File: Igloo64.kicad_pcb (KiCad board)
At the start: 2 copper layers, 96.5 x 90.2 mm, 31 parts, among them J1 Conn_02x32_Counter_Clockwise, J10 Conn_01x32, J11 Conn_01x02, J12 Conn_01x02, J13 Conn_01x02, J14 Conn_01x02, J15 Conn_01x02, J16 Conn_01x02, J17 Conn_01x02, J18 Conn_01x02, J19 Conn_01x02, J2 Conn_02x16_Odd_Even, J3 Conn_02x16_Odd_Even, J4 Conn_02x16_Odd_Even, J5 Conn_02x16_Odd_Even, J6 Conn_02x32_Odd_Even, J7 Conn_02x32_Odd_Even, J8 Conn_02x32_Odd_Even, J9 Conn_01x32

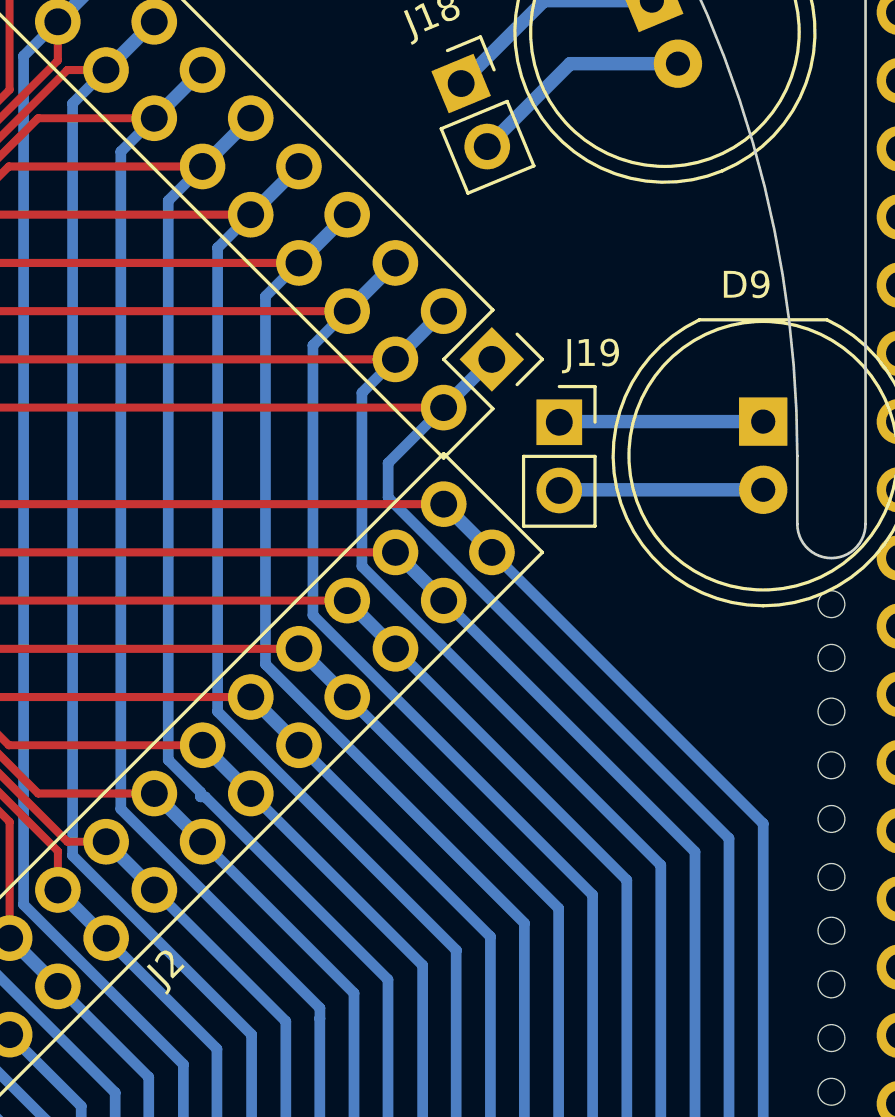
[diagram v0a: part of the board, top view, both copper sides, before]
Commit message: Fix DRC error.
One track too close to pin. Evened out some of the rear tracks for neatness.
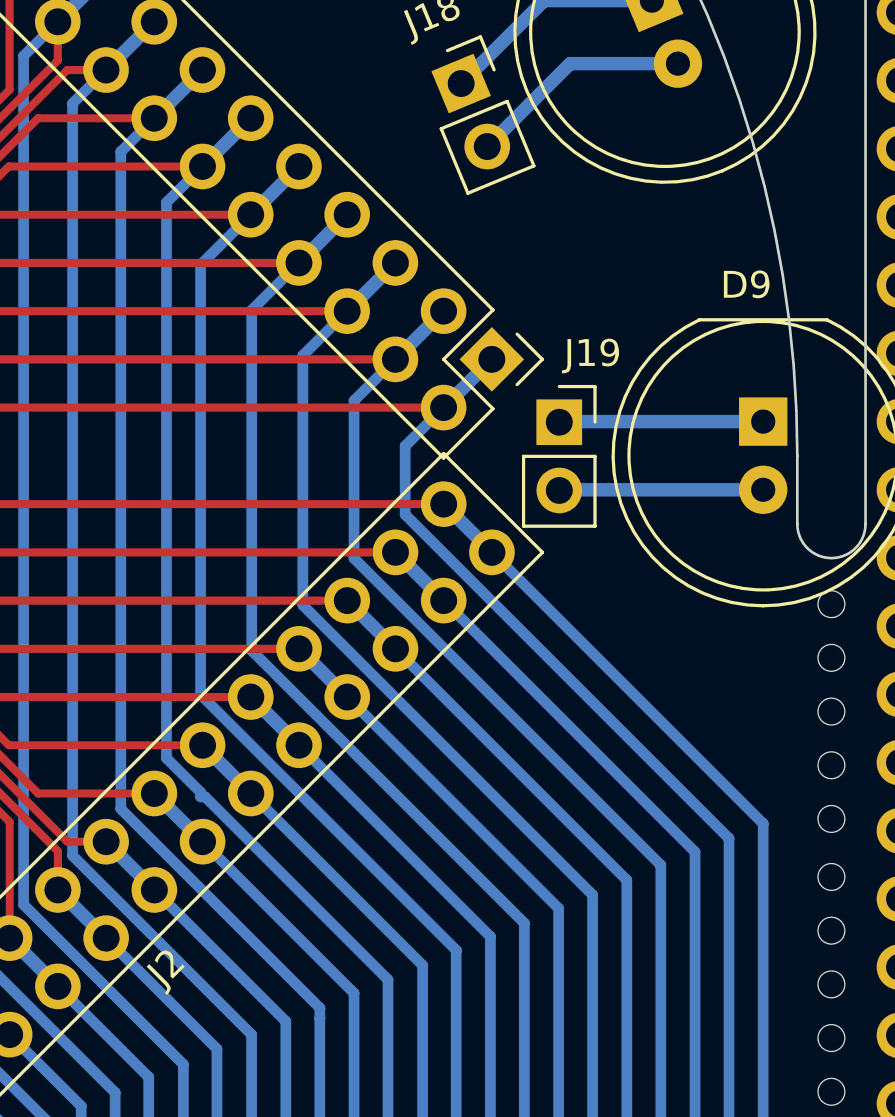
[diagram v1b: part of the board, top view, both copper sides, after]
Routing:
- net /pin37: track 82.1 -> 82.6 mm
- net /pin33: track 80.2 -> 79.7 mm
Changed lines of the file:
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@@
 	)
 	(segment
-		(start 158.75 90.454258)
-		(end 158.75 89.170769)
+		(start 159.385 91.089258)
+		(end 159.385 88.535769)
 		(width 0.4)
 		(layer "B.Cu")
@@
 	)
 	(segment
-		(start 171.445 125.735)
-		(end 171.445 103.149258)
+		(start 171.445 103.149258)
+		(end 159.385 91.089258)
 		(width 0.4)
 		(layer "B.Cu")
@@
 	)
 	(segment
-		(start 171.445 103.149258)
-		(end 158.75 90.454258)
+		(start 171.445 125.735)
+		(end 171.445 103.149258)
 		(width 0.4)
 		(layer "B.Cu")
@@
 	)
 	(segment
-		(start 162.612871 85.307898)
+		(start 159.385 88.535769)
 		(end 160.81682 87.103949)
-		(width 0.5)
+		(width 0.4)
 		(layer "B.Cu")
 		(net 4)
 	)
 	(segment
-		(start 158.75 89.170769)
+		(start 162.612871 85.307898)
 		(end 160.81682 87.103949)
-		(width 0.4)
+		(width 0.5)
 		(layer "B.Cu")
 		(net 4)
@@
 	)
 	(segment
-		(start 155.428666 81.715796)
-		(end 154.18269 82.961772)
-		(width 0.4)
-		(layer "B.Cu")
-		(net 22)
-	)
-	(segment
 		(start 157.224717 79.919744)
 		(end 155.428666 81.715795)
@@
 	)
 	(segment
-		(start 154.18269 96.663255)
+		(start 153.67 96.150565)
 		(end 163.825 106.305565)
 		(width 0.4)
@@
 	)
 	(segment
-		(start 154.18269 82.961772)
-		(end 154.18269 96.663255)
+		(start 153.67 83.474462)
+		(end 153.67 96.150565)
 		(width 0.4)
 		(layer "B.Cu")
@@
 	)
 	(segment
+		(start 155.428666 81.715796)
+		(end 153.67 83.474462)
+		(width 0.4)
+		(layer "B.Cu")
+		(net 22)
+	)
+	(segment
 		(start 138.028536 90.959449)
 		(end 141.360777 94.291689)
@@
 	)
 	(segment
-		(start 166.365 105.253463)
-		(end 166.365 125.735)
+		(start 155.575 94.463463)
+		(end 166.365 105.253463)
 		(width 0.4)
 		(layer "B.Cu")
@@
 	(segment
 		(start 157.224717 83.511847)
-		(end 155.949766 84.786798)
+		(end 155.575 85.161564)
 		(width 0.4)
 		(layer "B.Cu")
@@
 	)
 	(segment
-		(start 155.949766 84.786798)
-		(end 155.949766 94.838229)
+		(start 155.575 85.161564)
+		(end 155.575 94.463463)
 		(width 0.4)
 		(layer "B.Cu")
@@
 	)
 	(segment
-		(start 155.949766 94.838229)
-		(end 166.365 105.253463)
+		(start 166.365 105.253463)
+		(end 166.365 125.735)
 		(width 0.4)
 		(layer "B.Cu")
@@
 	)
 	(segment
-		(start 168.905 104.14341)
-		(end 168.905 125.735)
+		(start 157.48 92.71841)
+		(end 168.905 104.14341)
 		(width 0.4)
 		(layer "B.Cu")
@@
 	)
 	(segment
-		(start 157.774793 86.553874)
-		(end 157.774793 93.013203)
+		(start 168.905 104.14341)
+		(end 168.905 125.735)
 		(width 0.4)
 		(layer "B.Cu")
@@
 	)
 	(segment
-		(start 159.020769 85.307898)
-		(end 157.774793 86.553874)
+		(start 157.48 86.848667)
+		(end 157.48 92.71841)
 		(width 0.4)
 		(layer "B.Cu")
@@
 	)
 	(segment
-		(start 157.774793 93.013203)
-		(end 168.905 104.14341)
+		(start 159.020769 85.307898)
+		(end 157.48 86.848667)
 		(width 0.4)
 		(layer "B.Cu")
@@
 	)
 	(segment
-		(start 158.745 108.40977)
-		(end 158.745 125.735)
+		(start 151.765 101.42977)
+		(end 151.765 101.6)
 		(width 0.4)
 		(layer "B.Cu")
@@
 	)
 	(segment
-		(start 150.561613 100.226383)
-		(end 151.765 101.42977)
+		(start 150.495 79.465257)
+		(end 150.495 100.15977)
 		(width 0.4)
 		(layer "B.Cu")
@@
 	)
 	(segment
-		(start 151.836564 78.123693)
-		(end 150.561613 79.398644)
+		(start 158.745 108.40977)
+		(end 158.745 125.735)
 		(width 0.4)
 		(layer "B.Cu")
@@
 	)
 	(segment
-		(start 151.765 101.42977)
-		(end 151.765 101.6)
+		(start 151.93523 101.6)
+		(end 158.745 108.40977)
 		(width 0.4)
 		(layer "B.Cu")
@@
 	)
 	(segment
-		(start 150.561613 79.398644)
-		(end 150.561613 100.226383)
+		(start 150.495 100.15977)
+		(end 151.765 101.42977)
 		(width 0.4)
 		(layer "B.Cu")
@@
 	)
 	(segment
-		(start 151.93523 101.6)
-		(end 158.745 108.40977)
+		(start 151.836564 78.123693)
+		(end 150.495 79.465257)
 		(width 0.4)
 		(layer "B.Cu")
@@
 	)
 	(segment
-		(start 161.29 107.315)
-		(end 161.285 107.32)
+		(start 153.632615 79.919744)
+		(end 151.765 81.787359)
 		(width 0.4)
 		(layer "B.Cu")
@@
 	)
 	(segment
-		(start 161.285 107.32)
-		(end 161.285 125.735)
+		(start 161.29 107.315)
+		(end 161.285 107.32)
 		(width 0.4)
 		(layer "B.Cu")
@@
 	)
 	(segment
-		(start 152.4 98.425)
+		(start 151.765 97.79)
 		(end 161.29 107.315)
 		(width 0.4)
@@
 	)
 	(segment
-		(start 153.632615 79.919744)
-		(end 152.4 81.152359)
+		(start 161.285 107.32)
+		(end 161.285 125.735)
 		(width 0.4)
 		(layer "B.Cu")
@@
 	)
 	(segment
-		(start 152.4 81.152359)
-		(end 152.4 98.425)
+		(start 151.765 81.787359)
+		(end 151.765 97.79)
 		(width 0.4)
 		(layer "B.Cu")

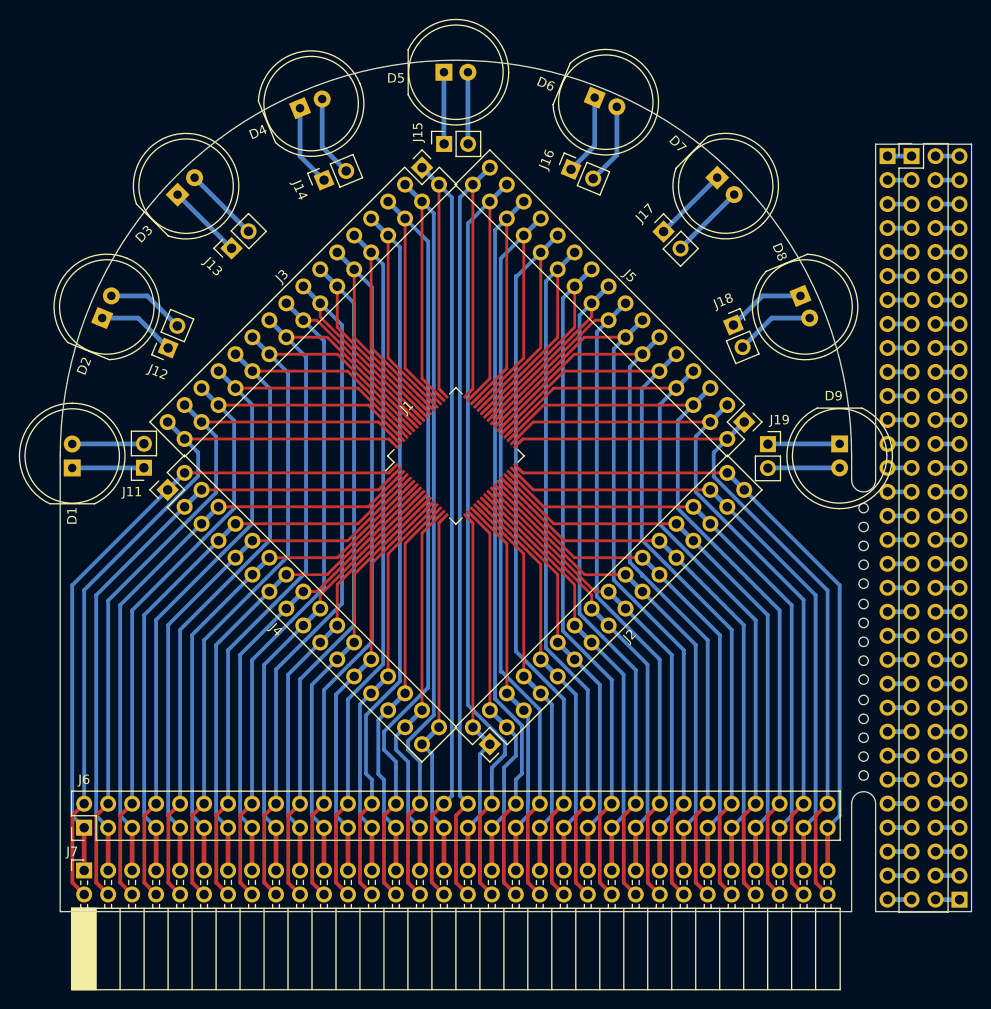
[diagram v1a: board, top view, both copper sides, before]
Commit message: Add silkscreen information.
Pin 1 arrow, logos, names, pin numbers, copyright date.
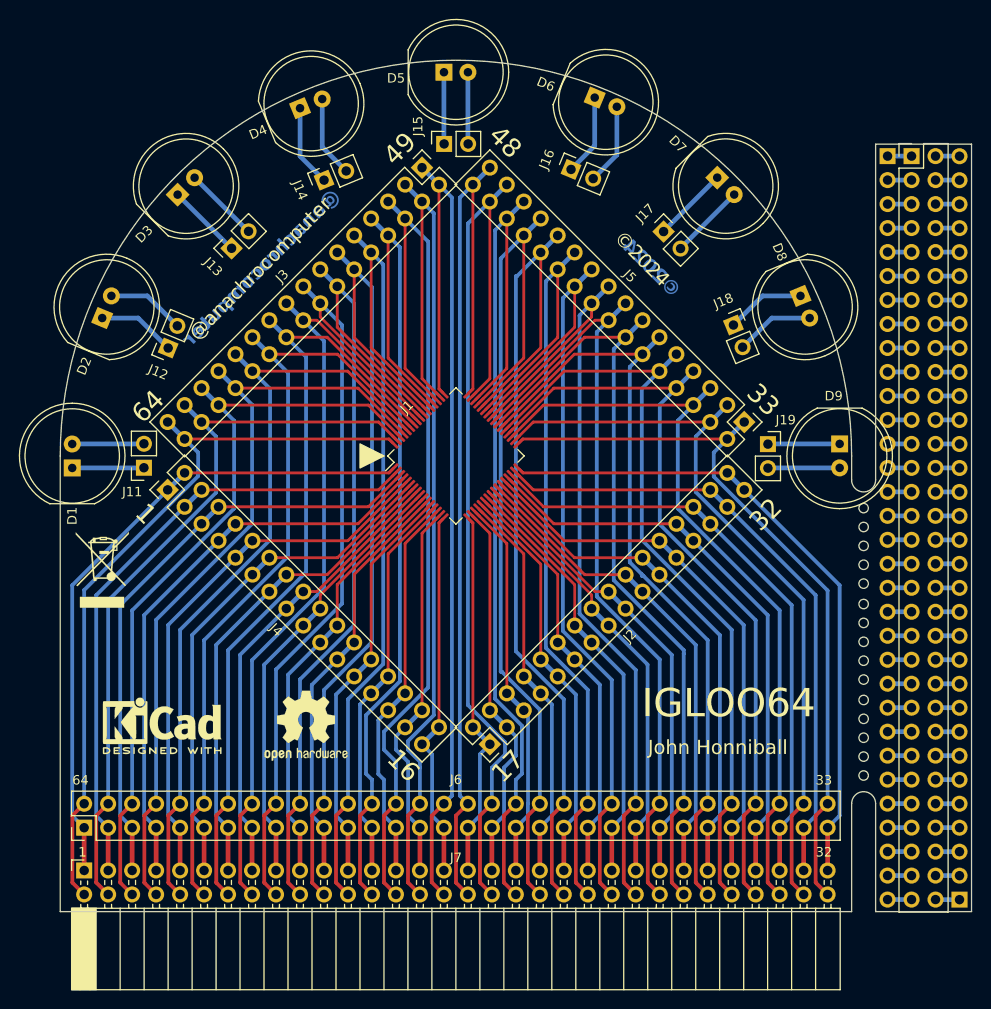
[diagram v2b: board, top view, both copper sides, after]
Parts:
- added REF**: KiCad-Logo2_5mm_SilkScreen, Symbol:KiCad-Logo2_5mm_SilkScreen, F.Cu at (101.0, 117.5)
- added REF**: OSHW-Logo2_9.8x8mm_SilkScreen, Symbol:OSHW-Logo2_9.8x8mm_SilkScreen, F.Cu at (116.2, 117.5)
- added REF**: WEEE-Logo_5.6x8mm_SilkScreen, Symbol:WEEE-Logo_5.6x8mm_SilkScreen, F.Cu at (94.6, 101.0)
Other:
- board text added: "1"
- board text added: "16"
- board text added: "17"
- board text added: "32"
- board text added: "33"
- board text added: "48"
- board text added: "49"
- board text added: "64"
- board text added: "@anachrocomputer"
- board text added: "IGLOO64"
- board text added: "John Honniball"
- board text added: "©2024"
